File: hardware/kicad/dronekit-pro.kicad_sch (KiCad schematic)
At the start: 30 parts, among them J101 2S-4S LiPo, Q101 AOD4185, U101 MP2307DN-LF-Z, U102 RT9013-33GB, U103 AP7361C-33E

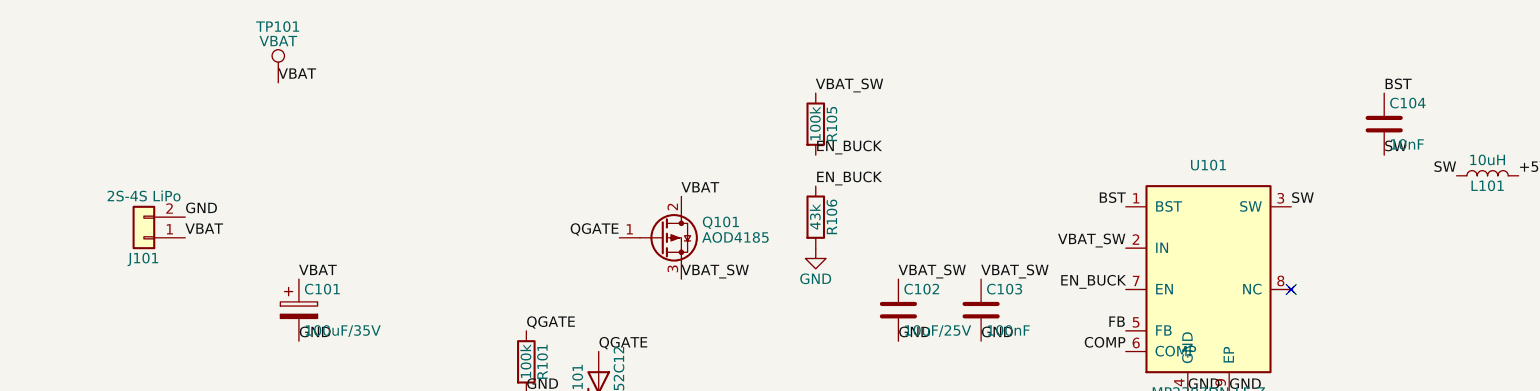
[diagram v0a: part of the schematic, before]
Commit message: Input spec 3S–4S LiPo; J101 relabelled, UVLO note near U101
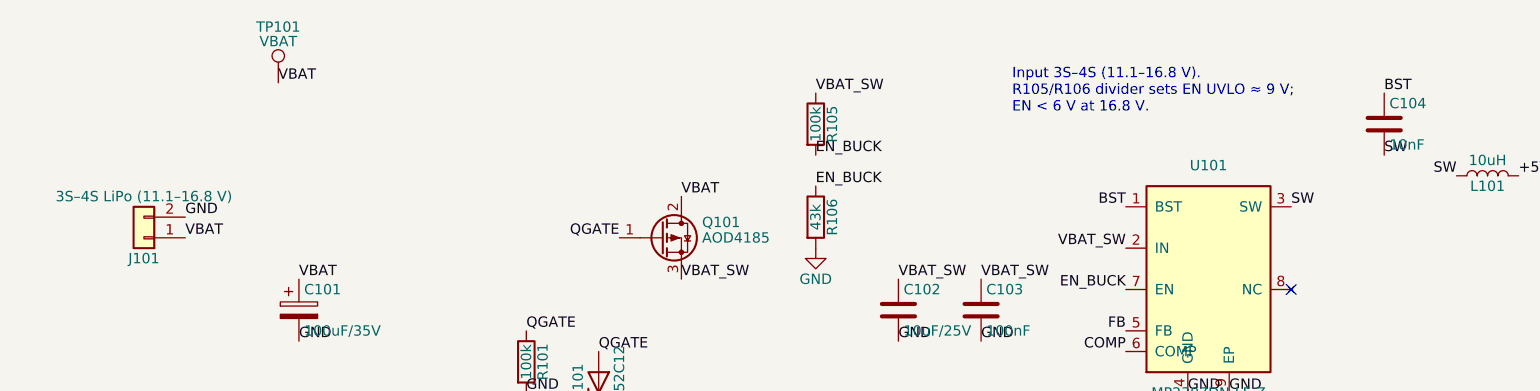
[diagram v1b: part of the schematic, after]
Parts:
- J101: value 2S-4S LiPo -> 3S–4S LiPo (11.1–16.8 V)
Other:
- note added: "Input 3S–4S (11.1–16.8 V). R105/R106 divider sets EN UVLO ≈ 9 V; EN < 6 V at 16.8 V."
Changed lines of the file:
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@@
 		)
 	)
+  (text "Input 3S–4S (11.1–16.8 V).\nR105/R106 divider sets EN UVLO ≈ 9 V;\nEN < 6 V at 16.8 V."
+    (at 146.05 95.25 0)
+    (effects (font (size 1.27 1.27)) (justify left bottom))
+  )
 	(symbol
 		(lib_id "Connector_Generic:Conn_01x02")
@@
 			)
 		)
-		(property "Value" "2S-4S LiPo"
+		(property "Value" "3S–4S LiPo (11.1–16.8 V)"
 			(at 39.37 105.41 0)
 			(effects
@@
 			)
 		)
-		(property "Description" "Generic connector, single row, 01x02, script generated (kicad-library-utils/schlib/autogen/connector/)"
+		(property "Description" "3S–4S LiPo (11.1–16.8 V)"
 			(at 39.37 110.49 0)
 			(hide yes)

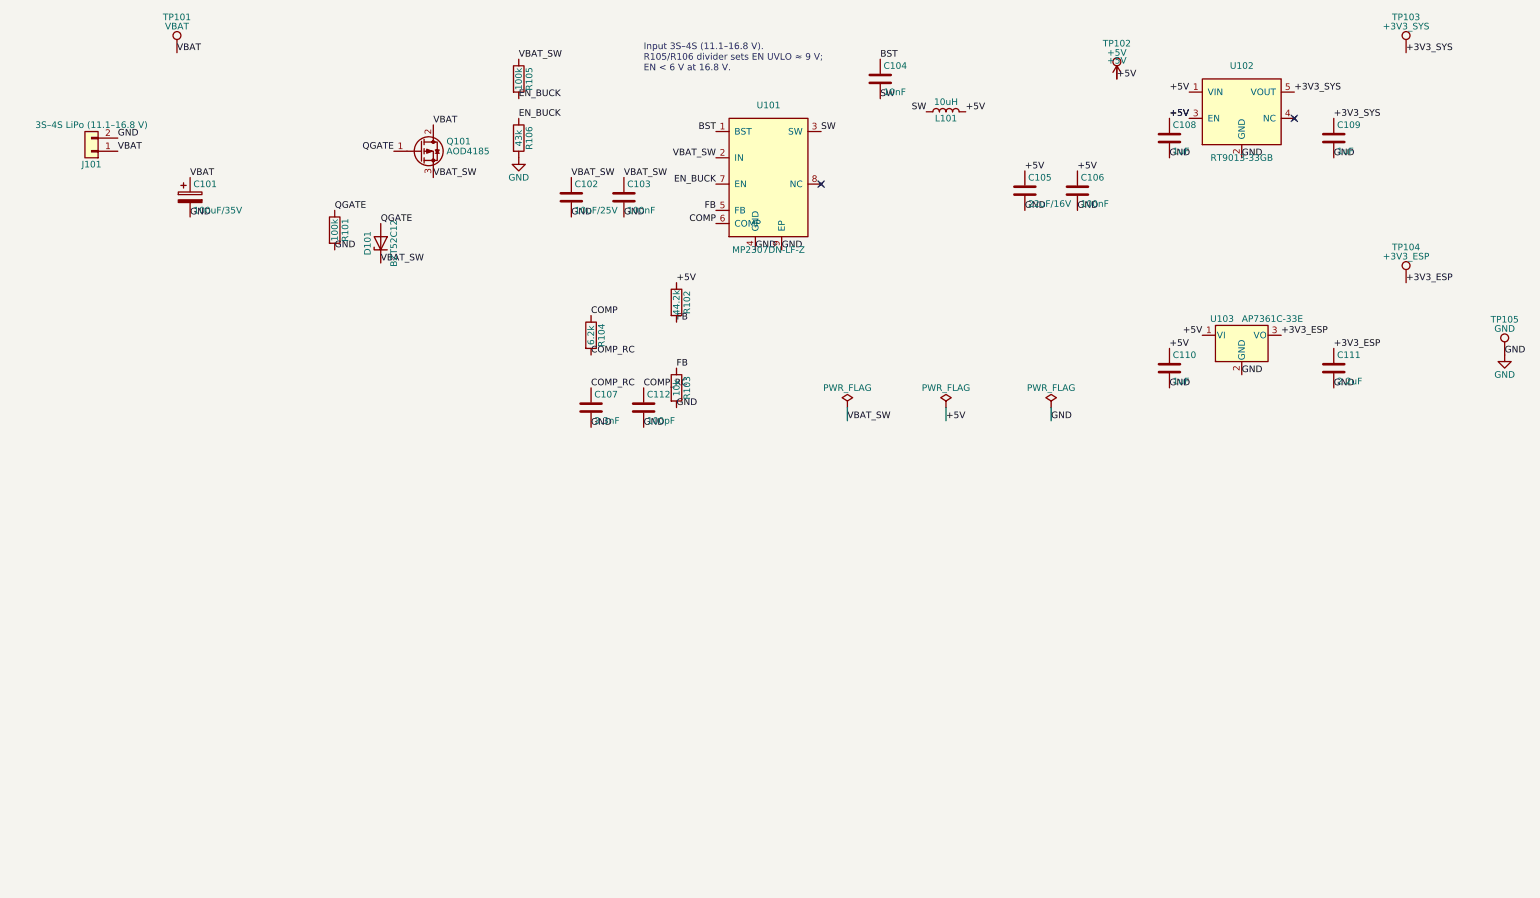
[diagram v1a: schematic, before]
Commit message: Block 2A: STM32F405 core sheet; Block 1 rails promoted to global
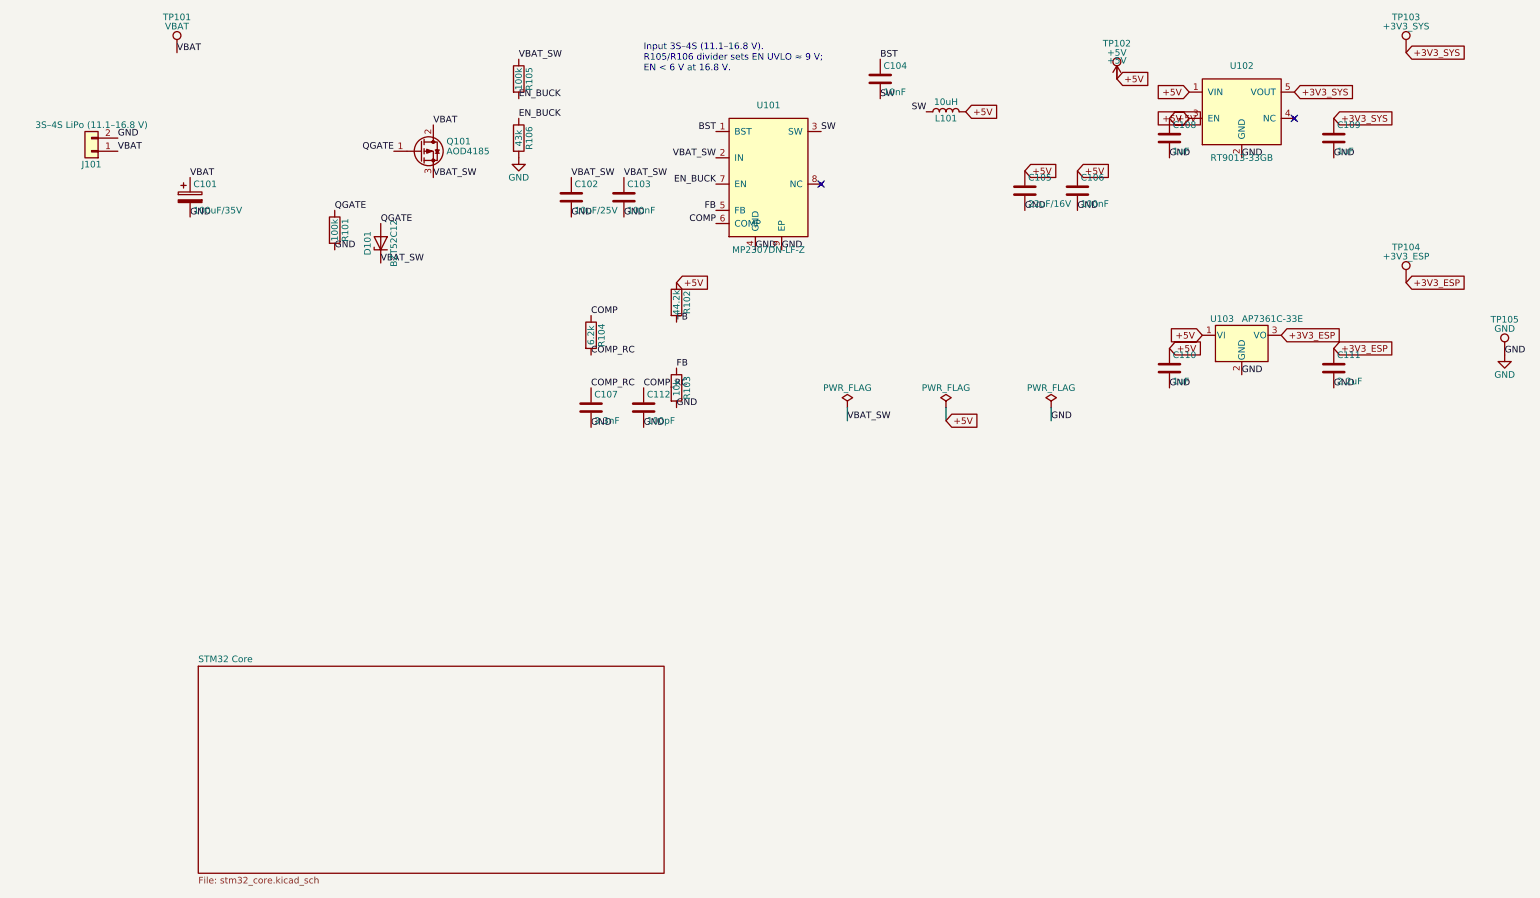
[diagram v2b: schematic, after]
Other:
- added sheet STM32 Core (stm32_core.kicad_sch)
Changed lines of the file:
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@@
 		)
 	)
-	(label "GND"
-		(at 44.45 107.95 0)
+	(text "Input 3S–4S (11.1–16.8 V).\nR105/R106 divider sets EN UVLO ≈ 9 V;\nEN < 6 V at 16.8 V."
+		(at 146.05 95.25 0)
 		(effects
 			(font
@@
 		)
 	)
-	(label "+5V"
-		(at 208.28 102.87 0)
-		(effects
-			(font
-				(size 1.27 1.27)
-			)
-			(justify left bottom)
-		)
-	)
-	(label "+5V"
-		(at 219.71 114.3 0)
-		(effects
-			(font
-				(size 1.27 1.27)
-			)
-			(justify left bottom)
-		)
-	)
-	(label "+5V"
-		(at 229.87 114.3 0)
-		(effects
-			(font
-				(size 1.27 1.27)
-			)
-			(justify left bottom)
-		)
-	)
-	(label "+5V"
-		(at 152.4 135.89 0)
-		(effects
-			(font
-				(size 1.27 1.27)
-			)
-			(justify left bottom)
-		)
-	)
-	(label "+5V"
-		(at 251.46 99.06 180)
-		(effects
-			(font
-				(size 1.27 1.27)
-			)
-			(justify right bottom)
-		)
-	)
-	(label "+5V"
-		(at 251.46 104.14 180)
-		(effects
-			(font
-				(size 1.27 1.27)
-			)
-			(justify right bottom)
-		)
-	)
-	(label "+5V"
-		(at 254 146.05 180)
-		(effects
-			(font
-				(size 1.27 1.27)
-			)
-			(justify right bottom)
-		)
-	)
-	(label "+5V"
-		(at 247.65 104.14 0)
-		(effects
-			(font
-				(size 1.27 1.27)
-			)
-			(justify left bottom)
-		)
-	)
-	(label "+5V"
-		(at 247.65 148.59 0)
-		(effects
-			(font
-				(size 1.27 1.27)
-			)
-			(justify left bottom)
-		)
-	)
-	(label "+5V"
-		(at 237.49 96.52 0)
-		(effects
-			(font
-				(size 1.27 1.27)
-			)
-			(justify left bottom)
-		)
-	)
 	(label "FB"
 		(at 160.02 121.92 180)
@@
 		)
 	)
-	(label "+3V3_SYS"
-		(at 271.78 99.06 0)
-		(effects
-			(font
-				(size 1.27 1.27)
-			)
-			(justify left bottom)
-		)
-	)
-	(label "+3V3_SYS"
-		(at 279.4 104.14 0)
-		(effects
-			(font
-				(size 1.27 1.27)
-			)
-			(justify left bottom)
-		)
-	)
-	(label "+3V3_SYS"
-		(at 293.37 91.44 0)
-		(effects
-			(font
-				(size 1.27 1.27)
-			)
-			(justify left bottom)
-		)
-	)
-	(label "+3V3_ESP"
-		(at 269.24 146.05 0)
-		(effects
-			(font
-				(size 1.27 1.27)
-			)
-			(justify left bottom)
-		)
-	)
-	(label "+3V3_ESP"
-		(at 279.4 148.59 0)
-		(effects
-			(font
-				(size 1.27 1.27)
-			)
-			(justify left bottom)
-		)
-	)
-	(label "+3V3_ESP"
-		(at 293.37 135.89 0)
-		(effects
-			(font
-				(size 1.27 1.27)
-			)
-			(justify left bottom)
-		)
-	)
 	(label "EN_BUCK"
 		(at 121.92 104.14 0)
@@
 		)
 	)
-	(label "+5V"
+	(label "GND"
+		(at 224.79 162.56 0)
+		(effects
+			(font
+				(size 1.27 1.27)
+			)
+			(justify left bottom)
+		)
+	)
+	(label "GND"
+		(at 44.45 107.95 0)
+		(effects
+			(font
+				(size 1.27 1.27)
+			)
+			(justify left bottom)
+		)
+	)
+	(global_label "+3V3_SYS"
+		(shape input)
+		(at 271.78 99.06 0)
+		(effects
+			(font
+				(size 1.27 1.27)
+			)
+			(justify left)
+		)
+	)
+	(global_label "+3V3_SYS"
+		(shape input)
+		(at 279.4 104.14 0)
+		(effects
+			(font
+				(size 1.27 1.27)
+			)
+			(justify left)
+		)
+	)
+	(global_label "+3V3_SYS"
+		(shape input)
+		(at 293.37 91.44 0)
+		(effects
+			(font
+				(size 1.27 1.27)
+			)
+			(justify left)
+		)
+	)
+	(global_label "+3V3_ESP"
+		(shape input)
+		(at 269.24 146.05 0)
+		(effects
+			(font
+				(size 1.27 1.27)
+			)
+			(justify left)
+		)
+	)
+	(global_label "+3V3_ESP"
+		(shape input)
+		(at 279.4 148.59 0)
+		(effects
+			(font
+				(size 1.27 1.27)
+			)
+			(justify left)
+		)
+	)
+	(global_label "+3V3_ESP"
+		(shape input)
+		(at 293.37 135.89 0)
+		(effects
+			(font
+				(size 1.27 1.27)
+			)
+			(justify left)
+		)
+	)
+	(global_label "+5V"
+		(shape input)
+		(at 208.28 102.87 0)
+		(effects
+			(font
+				(size 1.27 1.27)
+			)
+			(justify left)
+		)
+	)
+	(global_label "+5V"
+		(shape input)
+		(at 219.71 114.3 0)
+		(effects
+			(font
+				(size 1.27 1.27)
+			)
+			(justify left)
+		)
+	)
+	(global_label "+5V"
+		(shape input)
+		(at 229.87 114.3 0)
+		(effects
+			(font
+				(size 1.27 1.27)
+			)
+			(justify left)
+		)
+	)
+	(global_label "+5V"
+		(shape input)
+		(at 152.4 135.89 0)
+		(effects
+			(font
+				(size 1.27 1.27)
+			)
+			(justify left)
+		)
+	)
+	(global_label "+5V"
+		(shape input)
+		(at 251.46 99.06 180)
+		(effects
+			(font
+				(size 1.27 1.27)
+			)
+			(justify right)
+		)
+	)
+	(global_label "+5V"
+		(shape input)
+		(at 251.46 104.14 180)
+		(effects
+			(font
+				(size 1.27 1.27)
+			)
+			(justify right)
+		)
+	)
+	(global_label "+5V"
+		(shape input)
+		(at 254 146.05 180)
+		(effects
+			(font
+				(size 1.27 1.27)
+			)
+			(justify right)
+		)
+	)
+	(global_label "+5V"
+		(shape input)
+		(at 247.65 104.14 0)
+		(effects
+			(font
+				(size 1.27 1.27)
+			)
+			(justify left)
+		)
+	)
+	(global_label "+5V"
+		(shape input)
+		(at 247.65 148.59 0)
+		(effects
+			(font
+				(size 1.27 1.27)
+			)
+			(justify left)
+		)
+	)
+	(global_label "+5V"
+		(shape input)
+		(at 237.49 96.52 0)
+		(effects
+			(font
+				(size 1.27 1.27)
+			)
+			(justify left)
+		)
+	)
+	(global_label "+5V"
+		(shape input)
 		(at 204.47 162.56 0)
 		(effects
@@
 				(size 1.27 1.27)
 			)
-			(justify left bottom)
-		)
-	)
-	(label "GND"
-		(at 224.79 162.56 0)
-		(effects
-			(font
-				(size 1.27 1.27)
-			)
-			(justify left bottom)
-		)
-	)
-  (text "Input 3S–4S (11.1–16.8 V).\nR105/R106 divider sets EN UVLO ≈ 9 V;\nEN < 6 V at 16.8 V."
-    (at 146.05 95.25 0)
-    (effects (font (size 1.27 1.27)) (justify left bottom))
-  )
+			(justify left)
+		)
+	)
+	(sheet
+		(at 60 210)
+		(size 90 40)
+		(fields_autoplaced)
+		(stroke
+			(width 0.1524)
+			(type solid)
+		)
+		(fill
+			(color 0 0 0 0.0)
+		)
+		(property "Sheetname" "STM32 Core"
+			(at 60 209.365 0)
+			(effects
+				(font
+					(size 1.27 1.27)
+				)
+				(justify left bottom)
+			)
+		)
+		(property "Sheetfile" "stm32_core.kicad_sch"
+			(at 60 250.635 0)
+			(effects
+				(font
+					(size 1.27 1.27)
+				)
+				(justify left top)
+			)
+		)
+		(instances
+			(project "dronekit-pro"
+				(path "/8ff649ce-ea17-45ea-9d2f-8e238e021cf9"
+					(page "2")
+				)
+			)
+		)
+	)
 	(symbol
 		(lib_id "Connector_Generic:Conn_01x02")
